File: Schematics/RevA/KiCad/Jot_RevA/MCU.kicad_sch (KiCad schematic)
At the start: 7 parts, among them U1 MDBT50Q-1MV2, Y1 32.768kHz

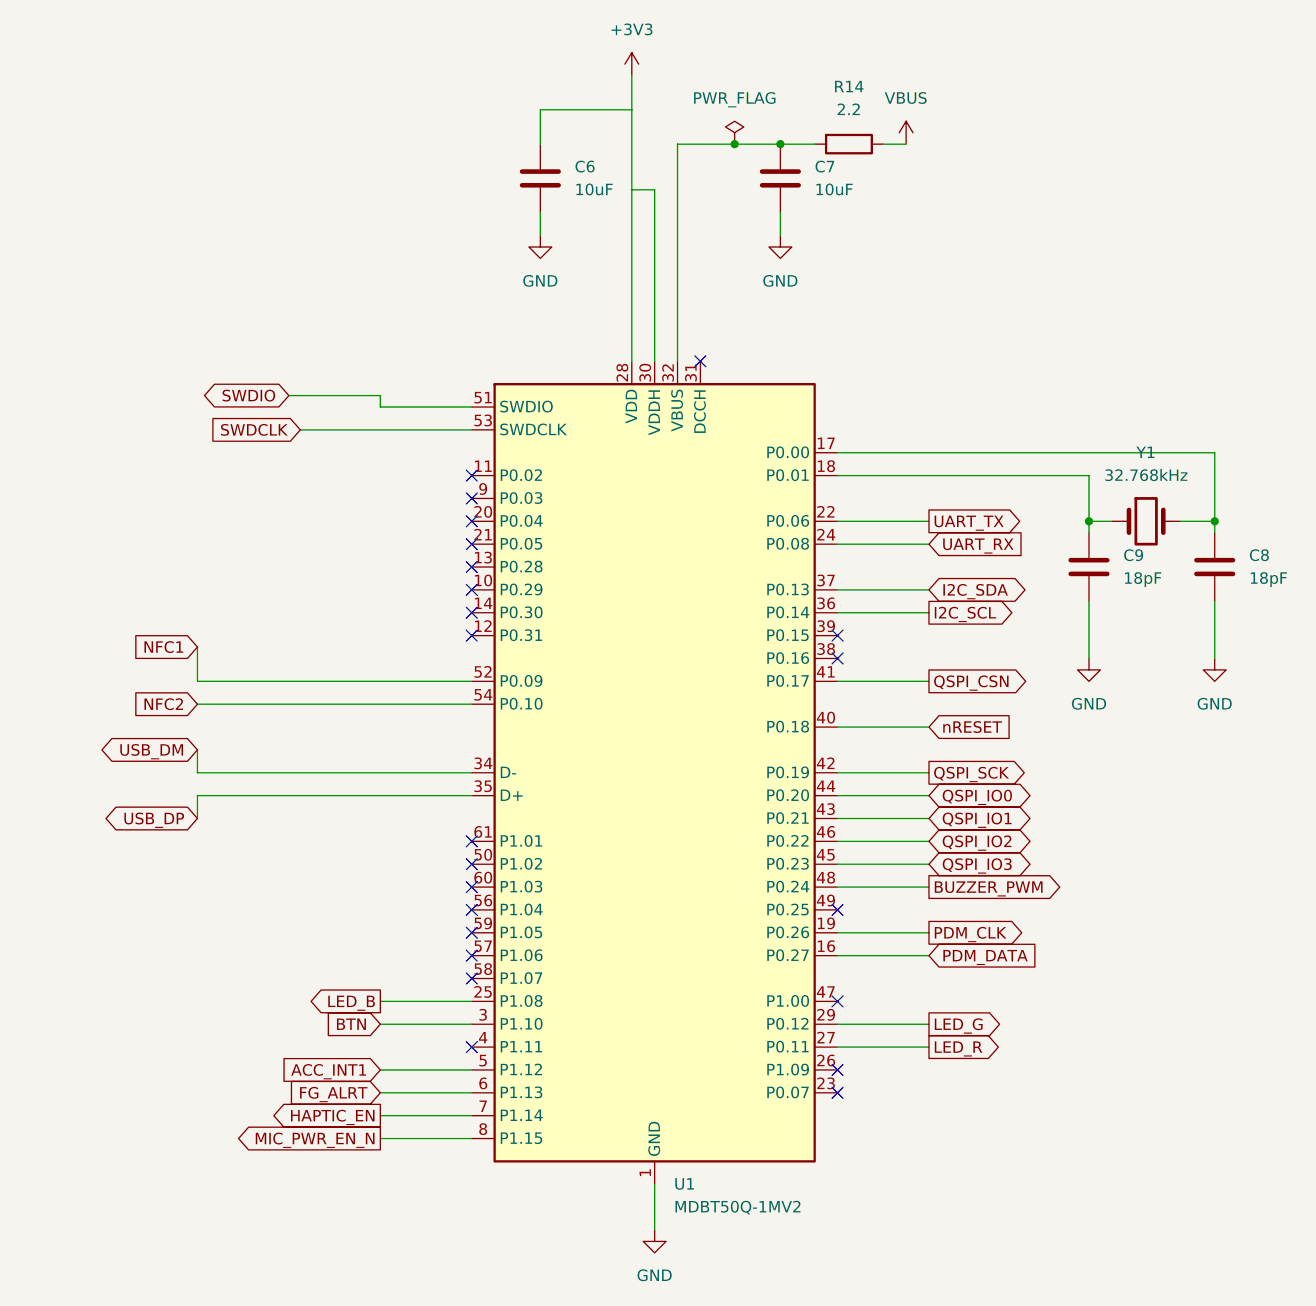
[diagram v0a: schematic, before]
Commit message: Rev A schematic final: battery fuse, reverse protection, VBUS TVS, charge inhibit, 32 MB flash
Polyfuse F1 and reverse-polarity P-FET Q6 between J2 and +BATT; SMF5.0A TVS on
VBUS; firmware charge inhibit (Q7/Q8, R20/R21, CHG_INHIBIT on P1.11, charging on
by default); R19 10R 1 W 2512; I2C pull-ups 2.2k; 1k series resistor on BTN;
flash W25Q256JVEIQ (symbol renamed); TP1/TP2/TP6 and J2 labels; junction dots.
BOM, pin list and architecture draft 5 updated (section 4.14: protection summary
and known Rev A limitations). JLCPCB upload BOM added. ERC clean.
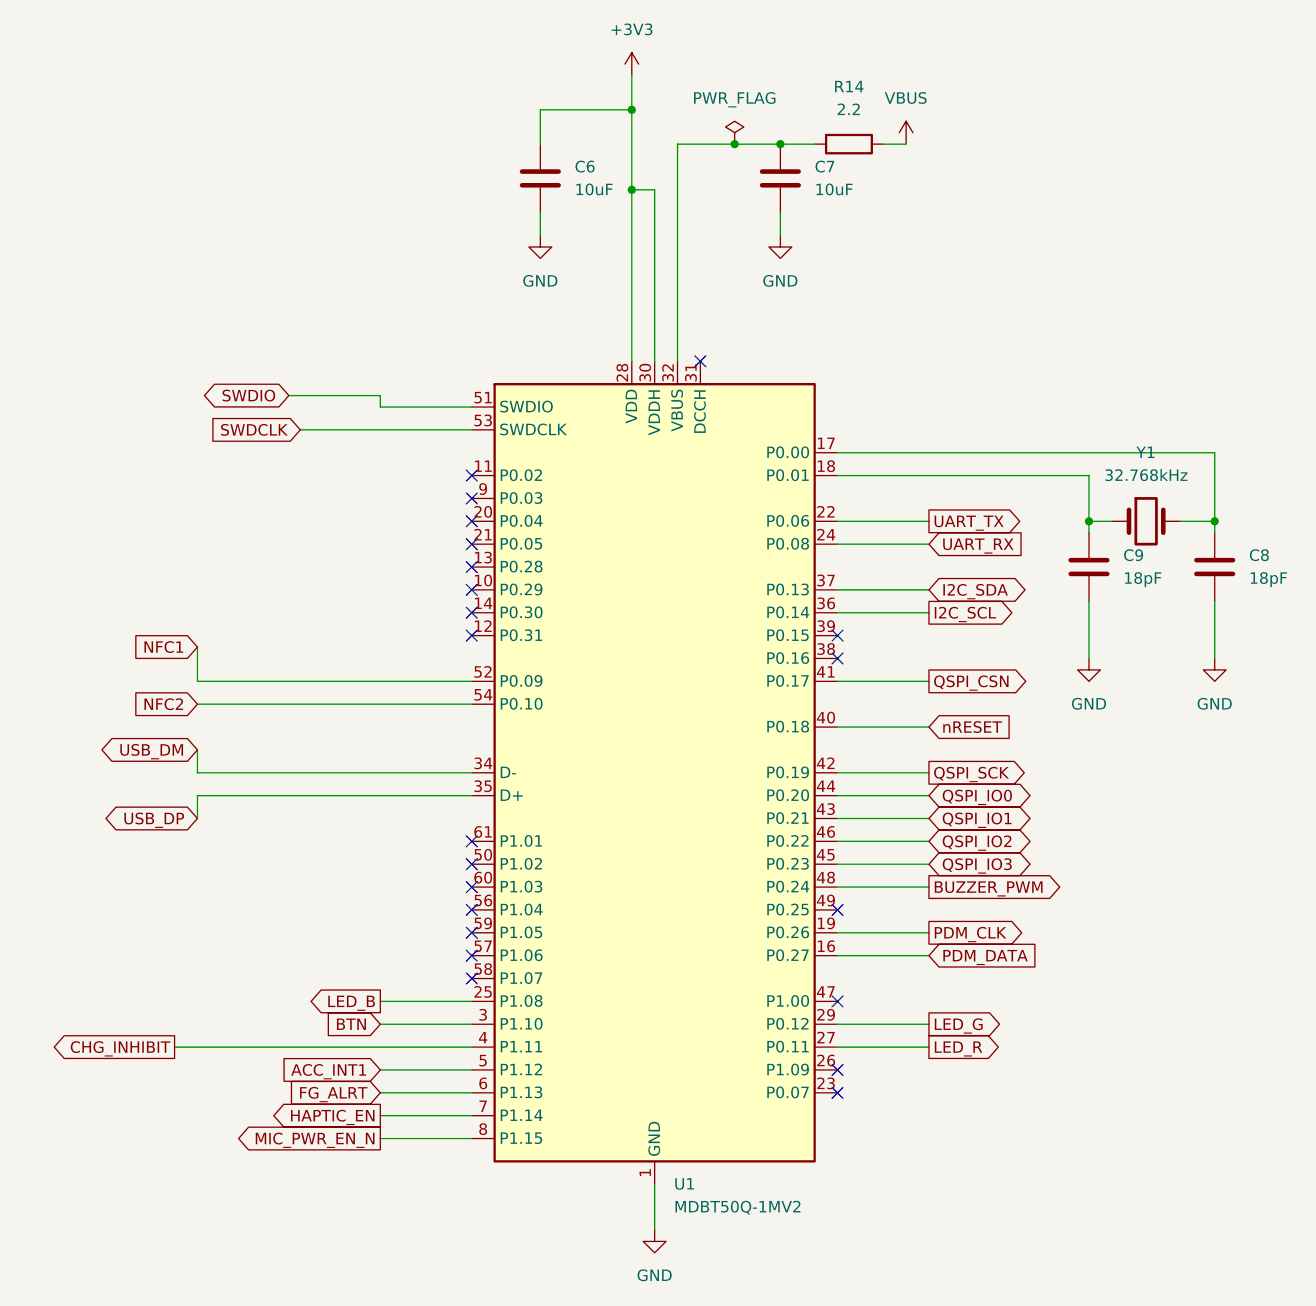
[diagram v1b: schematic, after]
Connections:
- net CHG_INHIBIT: now reaches U1.4 (P1.11)
- no-connect marks 23 -> 22
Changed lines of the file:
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@@
+	)
+	(junction
+		(at 139.7 36.83)
+		(diameter 0)
+		(color 0 0 0 0)
 	)
 	(junction
@@
 	)
 	(junction
+		(at 139.7 27.94)
+		(diameter 0)
+		(color 0 0 0 0)
+	)
+	(junction
 		(at 190.5 73.66)
 		(diameter 0)
@@
 	)
 	(no_connect
-		(at 121.92 132.08)
-	)
-	(no_connect
 		(at 121.92 76.2)
 	)
@@
 		(pts
 			(xy 121.92 142.24) (xy 111.76 142.24)
+		)
+		(stroke
+			(width 0)
+			(type default)
+		)
+	)
+	(wire
+		(pts
+			(xy 88.9 132.08) (xy 121.92 132.08)
 		)
 		(stroke
@@
 			(hide yes)
 			(show_name no)
+			(do_not_autoplace no)
+			(effects
+				(font
+					(size 1.27 1.27)
+				)
+				(justify right)
+			)
+		)
+	)
+	(global_label "CHG_INHIBIT"
+		(shape output)
+		(at 88.9 132.08 180)
+		(fields_autoplaced yes)
+		(effects
+			(font
+				(size 1.27 1.27)
+			)
+			(justify right)
+		)
+		(property "Intersheetrefs" "${INTERSHEET_REFS}"
+			(at 74.3637 132.08 0)
+			(hide yes)
+			(show_name no)

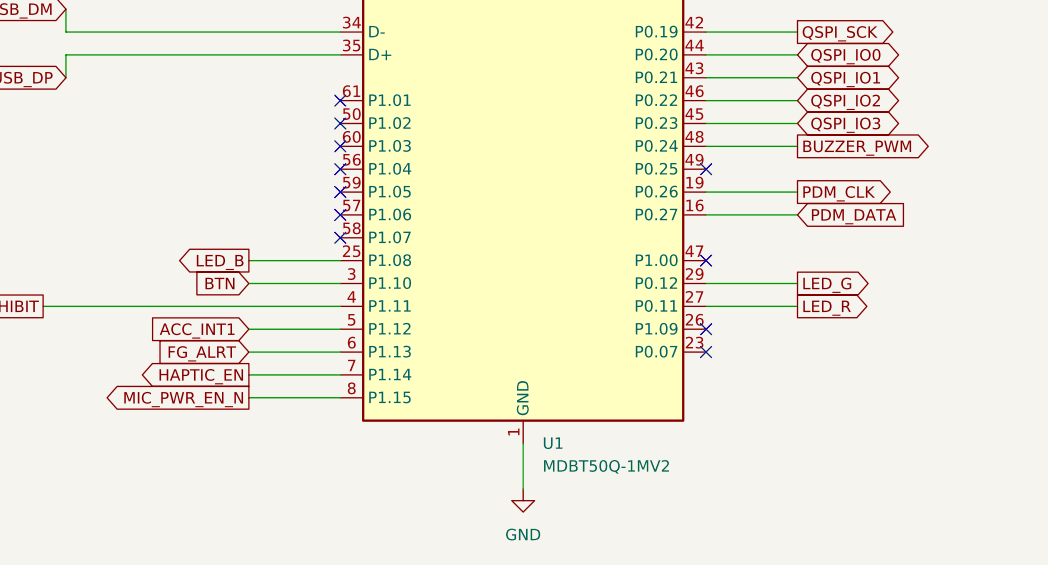
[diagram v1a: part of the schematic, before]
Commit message: Rev A layout complete: final routing and layout review fixes
- J2 is now two solder-wire holes (battery leads soldered): the JST-PH
  side-entry header is 5.5 mm tall and would not fit the 12.8 mm case.
  Removed from the JLCPCB BOM; BOM, architecture doc and case notes updated.
- LED drive pins re-assigned to match the transistor order:
  P1.08 red, P0.11 green, P0.12 blue. Pin list updated.
- No via drilled inside an SMD pad; no top-layer signal or via beside the
  crystal; 5 V branch removed from the power layer under the USB pair.
- R19 off the battery, C11 next to the mic, short ground vias at the
  module and decoupling capacitors, clean reset route.
- Silkscreen labels at 1.0 mm, battery + / - marked; zones refilled.
- DRC clean, board matches schematic, ERC clean.
- Case: 0.4 mm pocket over SW1, lip 0.8 mm.
- Architecture draft 7.
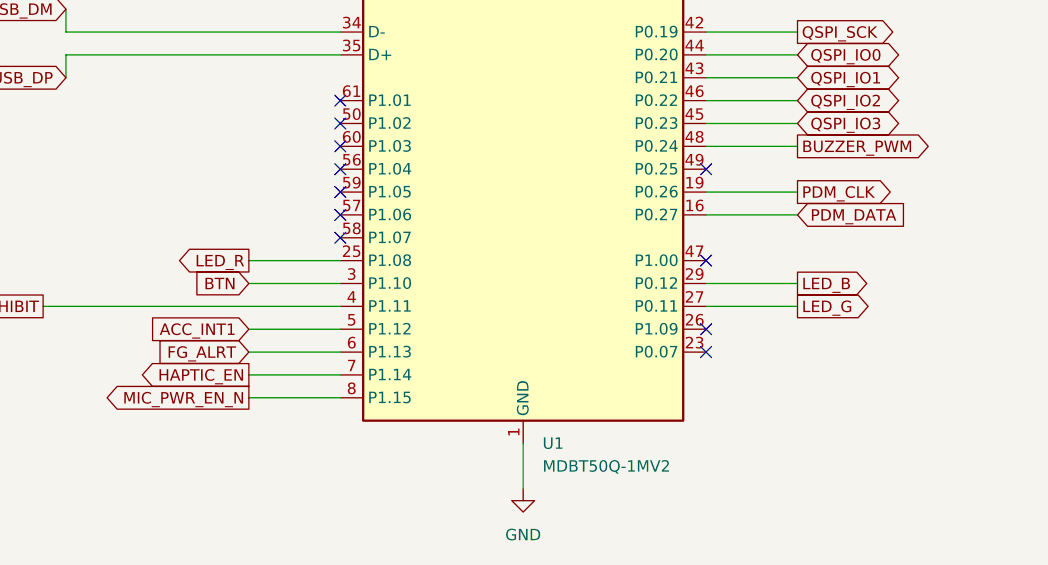
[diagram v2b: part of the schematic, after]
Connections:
- net LED_B: now also U1.29 (P0.12); no longer U1.25 (P1.08)
- net LED_G: now also U1.27 (P0.11); no longer U1.29 (P0.12)
- net LED_R: now also U1.25 (P1.08); no longer U1.27 (P0.11)
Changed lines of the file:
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@@
 		)
 	)
-	(global_label "LED_G"
+	(global_label "LED_B"
 		(shape output)
 		(at 172.72 129.54 0)
@@
 		)
 	)
-	(global_label "LED_R"
+	(global_label "LED_G"
 		(shape output)
 		(at 172.72 132.08 0)
@@
 		)
 	)
-	(global_label "LED_B"
+	(global_label "LED_R"
 		(shape output)
 		(at 111.76 127 180)
